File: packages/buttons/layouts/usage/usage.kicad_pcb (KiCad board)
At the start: 2 copper layers, 4 parts

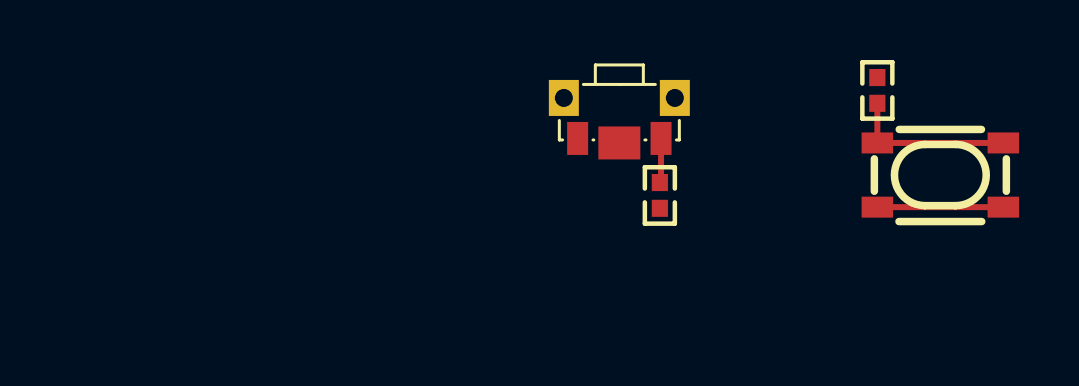
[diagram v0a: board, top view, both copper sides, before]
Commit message: update button layouts
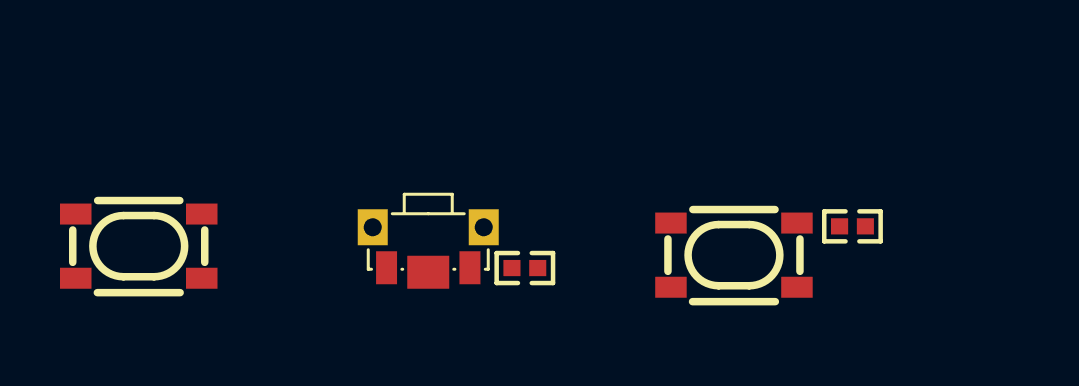
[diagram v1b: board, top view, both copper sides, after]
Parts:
- added SW3: , ALPSALPINE_SKTDLDE010:KEY-SMD_SKTDLDE010, F.Cu at (154.5, 86.8)
- SW1: footprint ALPSALPINE_SKTDLDE010:KEY-SMD_SKTDLDE010 -> ALPSALPINE_SKRPACE010:KEY-SMD_4P-L4.2-W3.2-P2.20-LS4.6
- moved SW1 16.6 mm to (144.9, 86.7)
- moved R2 13.2 mm to (157.8, 87.4), turned to 180 degrees
- moved SW2 7.38 mm to (164.7, 87.0)
- moved R1 6.50 mm to (168.7, 86.0), turned to 180 degrees
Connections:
- R1 pad 1: button-input-input-0 -> GND
- R1 pad 2: GND -> pulldown_signal
- R2 pad 1: button-input-input-1 -> VCC
- R2 pad 2: VCC -> pullup_signal
- SW1 pad 1: button-input-input-0 -> signal_a
- SW1 pad 2: button-output-output-0 -> signal_a
- SW1 pad 3: _3 -> signal_b
- SW1 pad 4: _4 -> signal_b
- SW2 pad 1: button-input-input-1 -> pulldown_signal
- SW2 pad 2: button-input-input-1 -> pulldown_signal
- SW2 pad 3: button-output-output-1 -> VCC
- SW2 pad 4: button-output-output-1 -> VCC
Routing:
- net button-input-input-1: track 5.52 -> 0.00 mm
- net button-output-output-1: track 4.20 -> 0.00 mm
- net button-input-input-0: track 1.49 -> 0.00 mm

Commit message: buttons: package update to v0.4.0, ato:^0.14.0 (#260)
* buttons: package update to v0.4.0, ato:^0.14.0

Build targets:
  HorizontalButton = rc0
  VerticalButton = rc0
  default = rc0
  usage = rc0
Package Verify: rc0
Version: 0.3.1 -> 0.4.0
Requires ato: ^0.14.0

* Update main.yml from main

Syncs GitHub Actions workflow configuration.

* ci: update workflow from main (fix package publish git issue)

* buttons: sync build outputs

Build targets:
  HorizontalButton = rc0
  VerticalButton = rc0
  usage = rc0
Package Verify: rc0

* manual fix package

* manual fix package

---------

Co-authored-by: Nicholas Krstevski <nick@atopile.io>
Co-authored-by: Nick Krstevski <51719418+nickkrstevski@users.noreply.github.com>
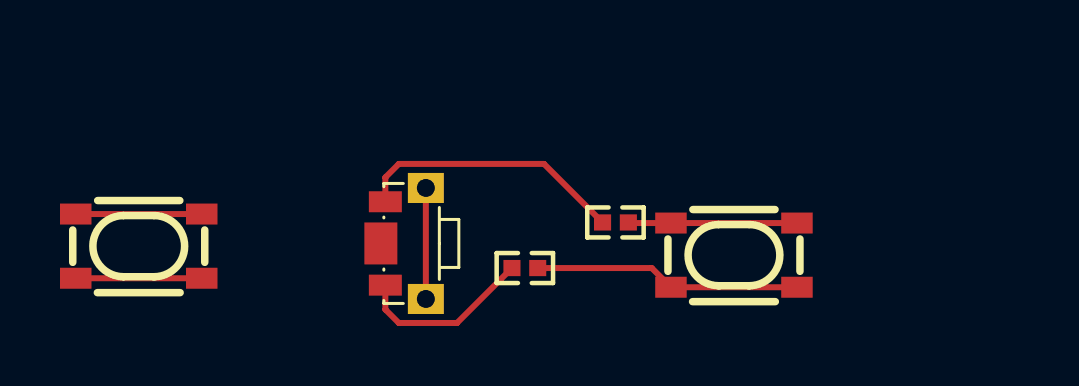
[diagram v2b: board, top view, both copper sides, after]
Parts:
- R1, R2: value 10kΩ ±1% 62.5mW -> 10000Ω
- moved R1 7.90 mm to (160.8, 85.9), turned to 0 degrees
- moved SW3 0.86 mm to (153.7, 86.6), turned to -90 degrees
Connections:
- net GND renamed lv
- net VCC renamed hv
- net _3 renamed 3
- net _4 renamed 4
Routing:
- net lv: track 0.00 -> 9.05 mm
- net hv: track 0.00 -> 8.91 mm
- net pullup_signal: track 0.00 -> 5.98 mm
- net pulldown_signal: track 0.00 -> 5.63 mm
- net signal_b: track 0.00 -> 4.20 mm
- net signal_a: track 0.00 -> 4.20 mm
- net 4: track 0.00 -> 3.70 mm
